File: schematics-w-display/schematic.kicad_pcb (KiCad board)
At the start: 2 copper layers, 59.8 x 61.5 mm, 8 parts, among them J1 Conn_01x21_Female, J2 Conn_01x06_Female, J3 Conn_01x21_Female, J4 Conn_01x08_Female

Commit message: Some schematic prettify
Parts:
- removed the   at (99.7, 114.7)
- added REF**: MountingHole_3.2mm_M3_DIN965, MountingHole:MountingHole_3.2mm_M3_DIN965, F.Cu at (99.7, 114.7)
- added SW1: SW_Push, Button_Switch_THT:SW_PUSH_6mm, F.Cu at (144.9, 74.6)
- added SW2: SW_Push, Button_Switch_THT:SW_Tactile_SKHH_Angled, F.Cu at (94.2, 120.2)
-  : value MountingHole_3.2mm_M3 -> MountingHole_3.2mm_M3_DIN965; footprint MountingHole:MountingHole_3.2mm_M3 -> MountingHole:MountingHole_3.2mm_M3_DIN965 (x3)
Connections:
- J1 pad 10: (no net) -> Net-(J1-Pad10)
- J1 pad 11: (no net) -> Net-(J1-Pad11)
- J1 pad 12: (no net) -> Net-(J1-Pad12)
- J1 pad 13: (no net) -> Net-(J1-Pad13)
- J1 pad 14: (no net) -> Net-(J1-Pad14)
- J1 pad 15: (no net) -> Net-(J1-Pad15)
- J1 pad 16: (no net) -> Net-(J1-Pad16)
- J1 pad 17: (no net) -> Net-(J1-Pad17)
- J1 pad 18: (no net) -> Net-(J1-Pad18)
- J1 pad 19: (no net) -> Net-(J1-Pad19)
- J1 pad 2: (no net) -> Net-(J1-Pad2)
- J1 pad 20: (no net) -> Net-(J1-Pad20)
- J1 pad 21: (no net) -> Net-(J1-Pad21)
- J1 pad 3: (no net) -> Net-(J1-Pad3)
- J1 pad 4: (no net) -> Net-(J1-Pad4)
- J1 pad 5: (no net) -> Net-(J1-Pad5)
- J1 pad 6: (no net) -> Net-(J1-Pad6)
- J1 pad 7: (no net) -> Net-(J1-Pad7)
- J1 pad 8: (no net) -> Net-(J1-Pad8)
- J1 pad 9: (no net) -> Net-(J1-Pad9)
- J3 pad 10: (no net) -> Net-(J3-Pad10)
- J3 pad 11: (no net) -> Net-(J3-Pad11)
- J3 pad 12: (no net) -> Net-(J3-Pad12)
- J3 pad 13: (no net) -> Net-(J3-Pad13)
- J3 pad 14: (no net) -> Net-(J3-Pad14)
- J3 pad 15: (no net) -> Net-(J3-Pad15)
- J3 pad 2: (no net) -> Net-(J3-Pad2)
- J3 pad 20: (no net) -> Net-(J3-Pad20)
- J3 pad 3: (no net) -> Net-(J3-Pad3)
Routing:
- net Net-(J1-Pad2): track 0.00 -> 93.9 mm
- net Net-(J3-Pad20): track 0.00 -> 48.0 mm

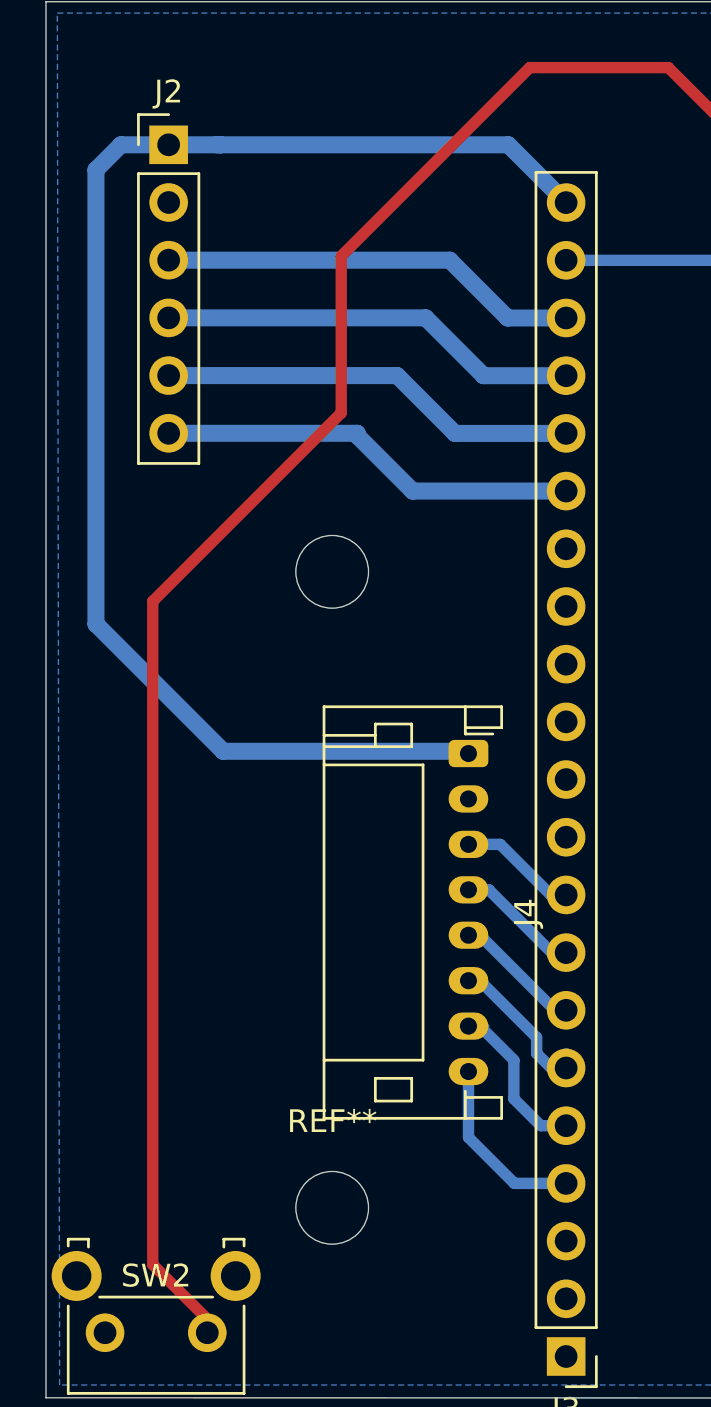
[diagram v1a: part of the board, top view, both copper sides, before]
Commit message: Add LDR to schematic
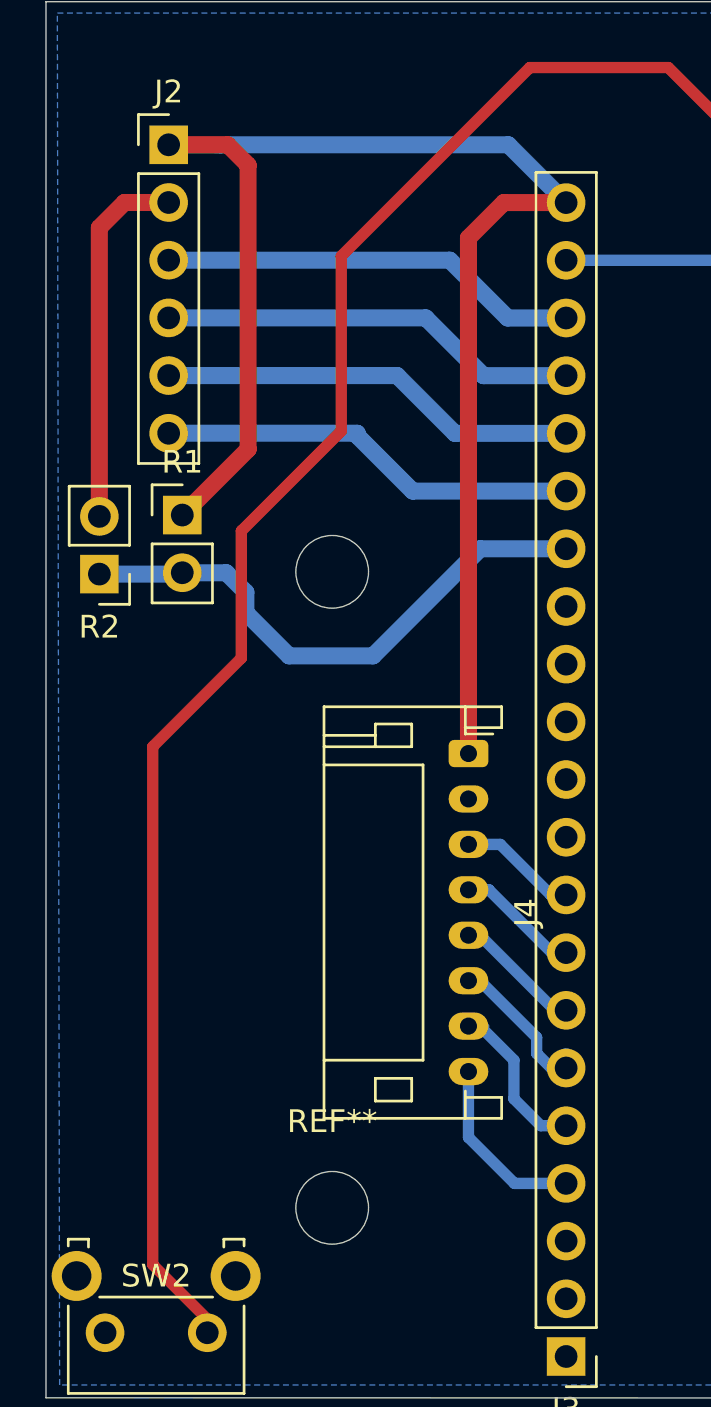
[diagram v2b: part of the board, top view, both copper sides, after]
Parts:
- added R1: LDR03, Connector_PinHeader_2.54mm:PinHeader_1x02_P2.54mm_Vertical, F.Cu at (93.1, 84.2)
- added R2: 10kOhm, Connector_PinHeader_2.54mm:PinHeader_1x02_P2.54mm_Vertical, F.Cu at (89.5, 86.8)
- J1, J3: value Conn_01x21_Female -> Conn_01x21_Female_ESP
- J2: value Conn_01x06_Female -> Conn_01x06_Female_BME280
- J4: value Conn_01x08_Female -> Conn_01x08_Female_Display
- SW1: value SW_Push -> Bootloader_Push
- SW2: value SW_Push -> RST_Push
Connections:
- net /3v3 renamed 3v3
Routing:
- net Net-(J3-Pad15): track 0.00 -> 24.7 mm
- net GND: track 0.00 -> 16.2 mm
- net 3v3: track 61.2 -> 67.0 mm

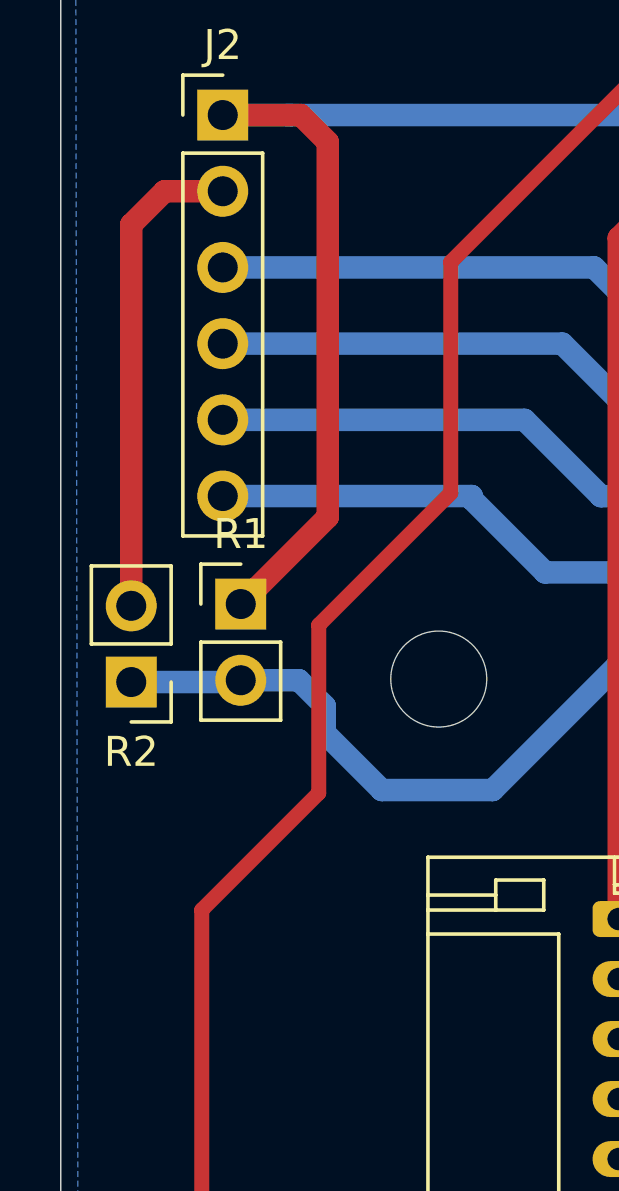
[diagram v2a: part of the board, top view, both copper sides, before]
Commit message: Use resistor as footprint for resistor
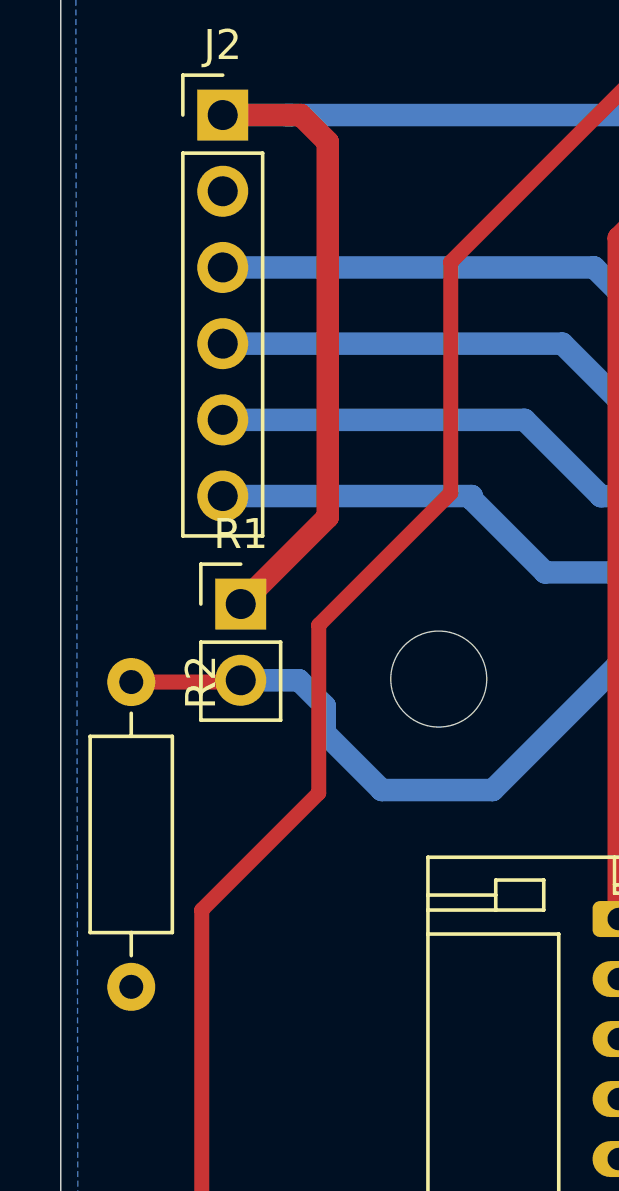
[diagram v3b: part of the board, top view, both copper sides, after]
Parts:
- R2: footprint Connector_PinHeader_2.54mm:PinHeader_1x02_P2.54mm_Vertical -> Resistor_THT:R_Axial_DIN0207_L6.3mm_D2.5mm_P10.16mm_Horizontal
- turned R2 to 270 degrees
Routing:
- net GND: track 16.2 -> 0.00 mm
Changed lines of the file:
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@@
     (thickness 1.6)
     (drawings 9)
-    (tracks 88)
+    (tracks 86)
     (zones 0)
     (modules 12)
@@
     (add_net "Net-(J3-Pad3)")
   )
-  (module Connector_PinHeader_2.54mm:PinHeader_1x02_P2.54mm_Vertical (layer F.Cu)
-    (at 89.45 86.8 180)
-    (descr "Through hole straight pin header, 1x02, 2.54mm pitch, single row")
-    (tags "Through hole pin header THT 1x02 2.54mm single row")
-    (fp_text reference R2 (at 0 -2.33) (layer F.SilkS)
-      (effects (font (size 1 1) (thickness 0.15)))
-    )
-    (fp_text value 10kOhm (at 5.95 1) (layer F.Fab)
-      (effects (font (size 1 1) (thickness 0.15)))
-    )
-    (fp_text user %R (at 0 1.27 90) (layer F.Fab)
-      (effects (font (size 1 1) (thickness 0.15)))
-    )
-    (fp_line (start -0.635 -1.27) (end 1.27 -1.27) (layer F.Fab) (width 0.1))
-    (fp_line (start 1.27 -1.27) (end 1.27 3.81) (layer F.Fab) (width 0.1))
-    (fp_line (start 1.27 3.81) (end -1.27 3.81) (layer F.Fab) (width 0.1))
-    (fp_line (start -1.27 3.81) (end -1.27 -0.635) (layer F.Fab) (width 0.1))
-    (fp_line (start -1.27 -0.635) (end -0.635 -1.27) (layer F.Fab) (width 0.1))
-    (fp_line (start -1.33 3.87) (end 1.33 3.87) (layer F.SilkS) (width 0.12))
-    (fp_line (start -1.33 1.27) (end -1.33 3.87) (layer F.SilkS) (width 0.12))
-    (fp_line (start 1.33 1.27) (end 1.33 3.87) (layer F.SilkS) (width 0.12))
-    (fp_line (start -1.33 1.27) (end 1.33 1.27) (layer F.SilkS) (width 0.12))
-    (fp_line (start -1.33 0) (end -1.33 -1.33) (layer F.SilkS) (width 0.12))
-    (fp_line (start -1.33 -1.33) (end 0 -1.33) (layer F.SilkS) (width 0.12))
-    (fp_line (start -1.8 -1.8) (end -1.8 4.35) (layer F.CrtYd) (width 0.05))
-    (fp_line (start -1.8 4.35) (end 1.8 4.35) (layer F.CrtYd) (width 0.05))
-    (fp_line (start 1.8 4.35) (end 1.8 -1.8) (layer F.CrtYd) (width 0.05))
-    (fp_line (start 1.8 -1.8) (end -1.8 -1.8) (layer F.CrtYd) (width 0.05))
-    (pad 2 thru_hole oval (at 0 2.54 180) (size 1.7 1.7) (drill 1) (layers *.Cu *.Mask)
+  (module Resistor_THT:R_Axial_DIN0207_L6.3mm_D2.5mm_P10.16mm_Horizontal (layer F.Cu)
+    (at 89.45 86.8 270)
+    (descr "Resistor, Axial_DIN0207 series, Axial, Horizontal, pin pitch=10.16mm, 0.25W = 1/4W, length*diameter=6.3*2.5mm^2, http://cdn-reichelt.de/documents/datenblatt/B400/1_4W%23YAG.pdf")
+    (tags "Resistor Axial_DIN0207 series Axial Horizontal pin pitch 10.16mm 0.25W = 1/4W length 6.3mm diameter 2.5mm")
+    (fp_text reference R2 (at 0 -2.33 90) (layer F.SilkS)
+      (effects (font (size 1 1) (thickness 0.15)))
+    )
+    (fp_text value 10kOhm (at 5.95 1 90) (layer F.Fab)
+      (effects (font (size 1 1) (thickness 0.15)))
+    )
+    (fp_text user %R (at 0 1.27) (layer F.Fab)
+      (effects (font (size 1 1) (thickness 0.15)))
+    )
+    (fp_line (start 1.93 -1.25) (end 1.93 1.25) (layer F.Fab) (width 0.1))
+    (fp_line (start 1.93 1.25) (end 8.23 1.25) (layer F.Fab) (width 0.1))
+    (fp_line (start 8.23 1.25) (end 8.23 -1.25) (layer F.Fab) (width 0.1))
+    (fp_line (start 8.23 -1.25) (end 1.93 -1.25) (layer F.Fab) (width 0.1))
+    (fp_line (start 0 0) (end 1.93 0) (layer F.Fab) (width 0.1))
+    (fp_line (start 10.16 0) (end 8.23 0) (layer F.Fab) (width 0.1))
+    (fp_line (start 1.81 -1.37) (end 1.81 1.37) (layer F.SilkS) (width 0.12))
+    (fp_line (start 1.81 1.37) (end 8.35 1.37) (layer F.SilkS) (width 0.12))
+    (fp_line (start 8.35 1.37) (end 8.35 -1.37) (layer F.SilkS) (width 0.12))
+    (fp_line (start 8.35 -1.37) (end 1.81 -1.37) (layer F.SilkS) (width 0.12))
+    (fp_line (start 1.04 0) (end 1.81 0) (layer F.SilkS) (width 0.12))
+    (fp_line (start 9.12 0) (end 8.35 0) (layer F.SilkS) (width 0.12))
+    (fp_line (start -1.05 -1.5) (end -1.05 1.5) (layer F.CrtYd) (width 0.05))
+    (fp_line (start -1.05 1.5) (end 11.21 1.5) (layer F.CrtYd) (width 0.05))
+    (fp_line (start 11.21 1.5) (end 11.21 -1.5) (layer F.CrtYd) (width 0.05))
+    (fp_line (start 11.21 -1.5) (end -1.05 -1.5) (layer F.CrtYd) (width 0.05))
+    (pad 2 thru_hole oval (at 10.16 0 270) (size 1.6 1.6) (drill 0.8) (layers *.Cu *.Mask)
       (net 5 GND))
-    (pad 1 thru_hole rect (at 0 0 180) (size 1.7 1.7) (drill 1) (layers *.Cu *.Mask)
+    (pad 1 thru_hole circle (at 0 0 270) (size 1.6 1.6) (drill 0.8) (layers *.Cu *.Mask)
       (net 33 "Net-(J3-Pad15)"))
-    (model ${KISYS3DMOD}/Connector_PinHeader_2.54mm.3dshapes/PinHeader_1x02_P2.54mm_Vertical.wrl
+    (model ${KISYS3DMOD}/Resistor_THT.3dshapes/R_Axial_DIN0207_L6.3mm_D2.5mm_P10.16mm_Horizontal.wrl
       (at (xyz 0 0 0))
       (scale (xyz 1 1 1))
@@
   (segment (start 103.245 83.145) (end 110 83.145) (width 0.75) (layer B.Cu) (net 4))
   (segment (start 100.8 80.7) (end 103.245 83.145) (width 0.75) (layer B.Cu) (net 4))
-  (segment (start 89.45 84.26) (end 89.45 71.55) (width 0.75) (layer F.Cu) (net 5))
-  (segment (start 90.56 70.44) (end 92.5 70.44) (width 0.75) (layer F.Cu) (net 5))
-  (segment (start 89.45 71.55) (end 90.56 70.44) (width 0.75) (layer F.Cu) (net 5))
   (segment (start 109.935 100.9) (end 110 100.965) (width 0.75) (layer B.Cu) (net 6))
   (segment (start 110 100.925) (end 109.525 100.925) (width 0.75) (layer B.Cu) (net 6))
@@
   (segment (start 140.4 74.6) (end 140.4 81.1) (width 0.5) (layer B.Cu) (net 32))
   (segment (start 89.7 86.8) (end 89.45 86.8) (width 0.75) (layer B.Cu) (net 33))
-  (segment (start 89.45 86.8) (end 93.04 86.8) (width 0.75) (layer B.Cu) (net 33))
   (segment (start 93.1 86.74) (end 95.04 86.74) (width 0.75) (layer B.Cu) (net 33))
   (segment (start 95.04 86.74) (end 95.9 87.6) (width 0.75) (layer B.Cu) (net 33))
@@
   (segment (start 106.215 85.685) (end 110 85.685) (width 0.75) (layer B.Cu) (net 33))
   (segment (start 101.5 90.4) (end 106.215 85.685) (width 0.75) (layer B.Cu) (net 33))
+  (segment (start 93.04 86.8) (end 93.1 86.74) (width 0.5) (layer F.Cu) (net 33))
+  (segment (start 89.45 86.8) (end 93.04 86.8) (width 0.5) (layer F.Cu) (net 33))
   (segment (start 110 70.445) (end 107.255 70.445) (width 0.75) (layer F.Cu) (net 41))
   (segment (start 105.7 72) (end 105.7 94.7) (width 0.75) (layer F.Cu) (net 41))

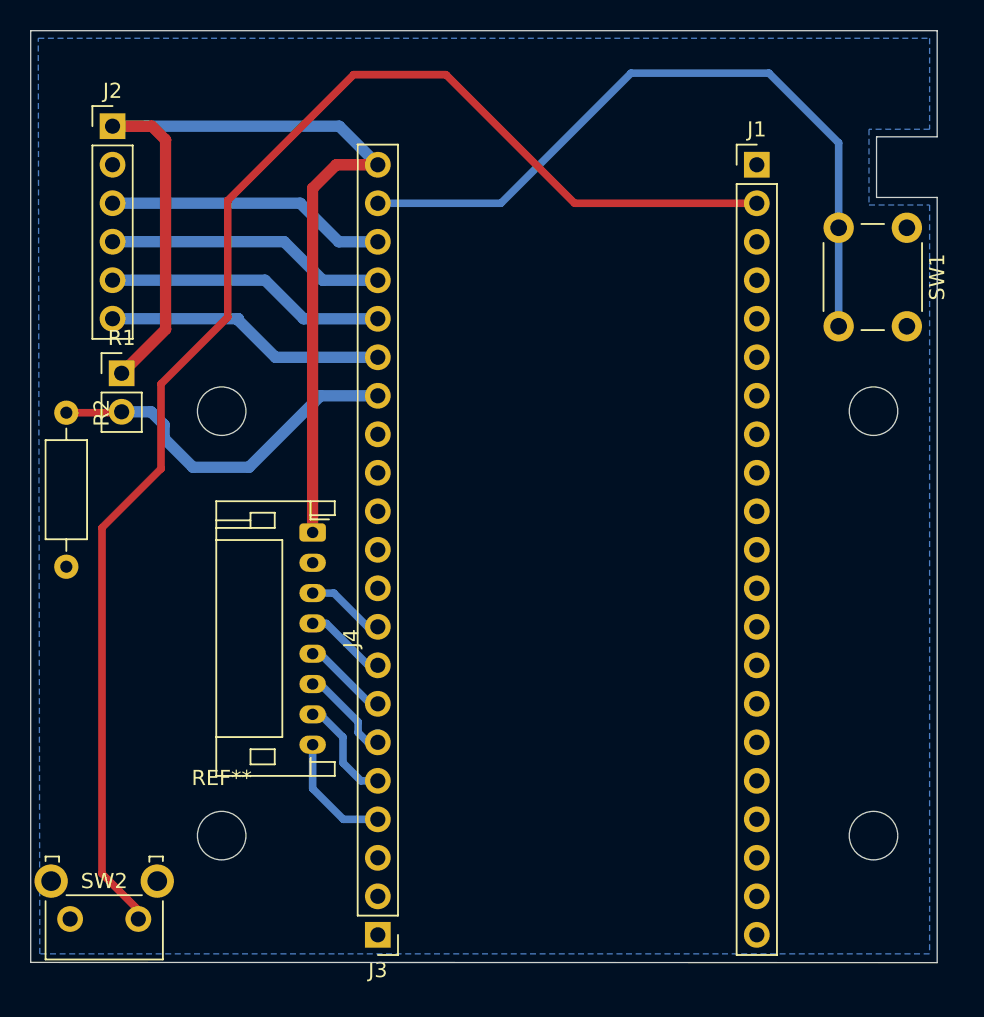
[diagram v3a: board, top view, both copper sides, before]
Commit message: New version of display pcb
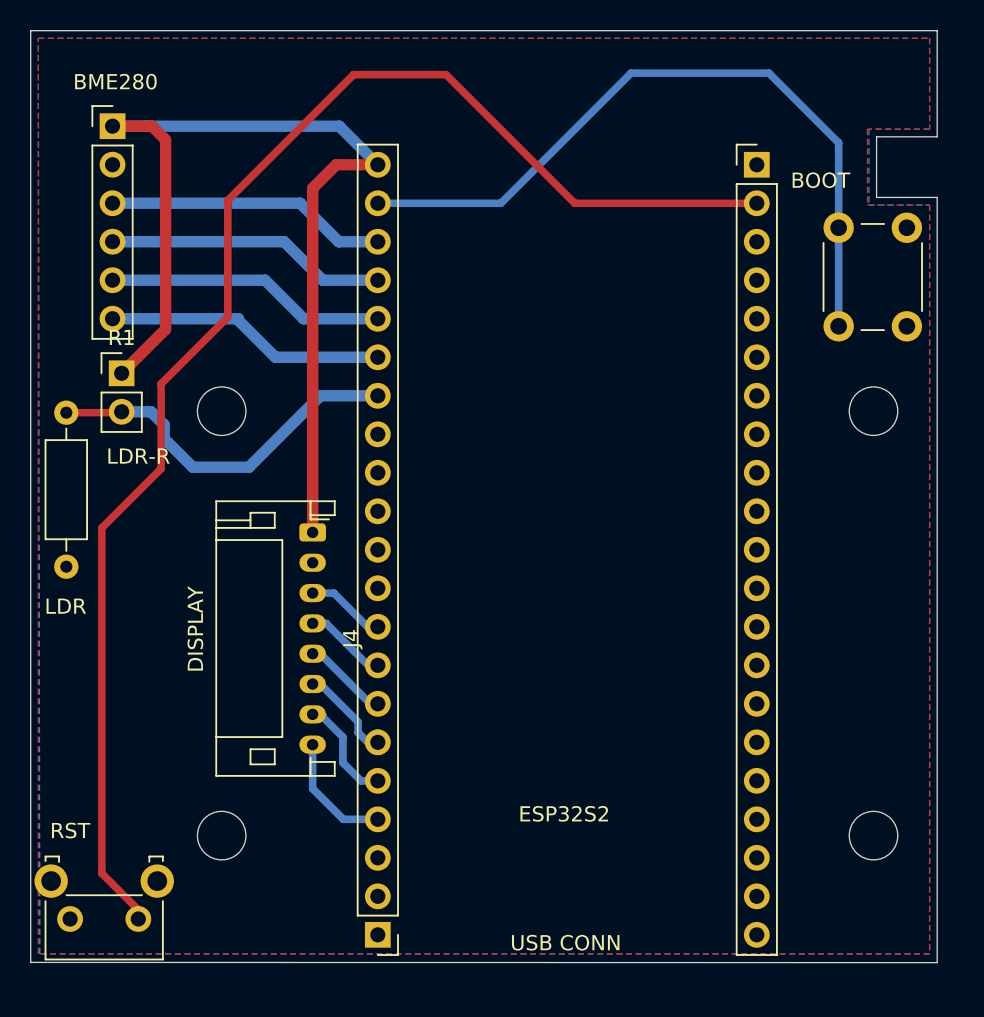
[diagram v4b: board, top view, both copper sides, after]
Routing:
- added copper zone on F.Cu, net GND
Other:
- board text added: "BME280"
- board text added: "BOOT"
- board text added: "DISPLAY"
- board text added: "ESP32S2"
- board text added: "LDR"
- board text added: "LDR-R"
- board text added: "RST"
- board text added: "USB CONN"
